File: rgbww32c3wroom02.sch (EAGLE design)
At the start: 21 parts, among them IC2 7805TV

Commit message: some corrections before production
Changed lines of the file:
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@@
 <instance part="R10" gate="G$1" x="-2.54" y="7.62" rot="R90"/>
 <instance part="GND1" gate="1" x="-55.88" y="114.3"/>
-<instance part="GND3" gate="1" x="-45.72" y="78.74"/>
+<instance part="GND3" gate="1" x="-55.88" y="73.66"/>
 <instance part="RST" gate="G$1" x="-88.9" y="78.74" smashed="yes">
 <attribute name="NAME" x="-83.82" y="76.2" size="1.778" layer="95" rot="R180"/>
@@
 <attribute name="VALUE" x="-101.6" y="35.56" size="1.778" layer="96"/>
 </instance>
-<instance part="U$5" gate="G$1" x="-63.5" y="63.5"/>
+<instance part="U$5" gate="G$1" x="-58.42" y="53.34"/>
 </instances>
 <busses>
@@
 </segment>
 <segment>
-<wire x1="-53.34" y1="81.28" x2="-45.72" y2="81.28" width="0.1524" layer="91"/>
+<wire x1="-60.96" y1="73.66" x2="-55.88" y2="76.2" width="0.1524" layer="91"/>
 <pinref part="GND3" gate="1" pin="GND"/>
 <pinref part="U$5" gate="G$1" pin="GND"/>
@@
 <net name="CLR" class="0">
 <segment>
-<wire x1="-40.64" y1="48.26" x2="-25.4" y2="48.26" width="0.1524" layer="91"/>
-<label x="-25.4" y="48.26" size="1.4224" layer="95" xref="yes"/>
+<wire x1="-48.26" y1="53.34" x2="-33.02" y2="53.34" width="0.1524" layer="91"/>
+<label x="-33.02" y="53.34" size="1.4224" layer="95" xref="yes"/>
 <pinref part="U$5" gate="G$1" pin="IO18"/>
 </segment>
@@
 <net name="N$5" class="0">
 <segment>
-<wire x1="-40.64" y1="63.5" x2="-25.4" y2="63.5" width="0.1524" layer="91"/>
-<label x="-25.4" y="63.5" size="1.4224" layer="95" xref="yes"/>
+<wire x1="-48.26" y1="60.96" x2="-38.1" y2="60.96" width="0.1524" layer="91"/>
+<label x="-38.1" y="60.96" size="1.4224" layer="95" xref="yes"/>
 <pinref part="U$5" gate="G$1" pin="I02"/>
 </segment>
@@
 <net name="N$9" class="0">
 <segment>
-<wire x1="-40.64" y1="53.34" x2="-25.4" y2="53.34" width="0.1524" layer="91"/>
-<label x="-25.4" y="53.34" size="1.4224" layer="95" xref="yes"/>
+<wire x1="-48.26" y1="55.88" x2="-38.1" y2="55.88" width="0.1524" layer="91"/>
+<label x="-38.1" y="55.88" size="1.4224" layer="95" xref="yes"/>
 <pinref part="U$5" gate="G$1" pin="IO19"/>
 </segment>
@@
 </segment>
 <segment>
-<wire x1="-60.96" y1="81.28" x2="-60.96" y2="88.9" width="0.1524" layer="91"/>
-<label x="-60.96" y="88.9" size="1.4224" layer="95" rot="R90" xref="yes"/>
+<wire x1="-63.5" y1="73.66" x2="-63.5" y2="78.74" width="0.1524" layer="91"/>
+<label x="-63.5" y="78.74" size="1.4224" layer="95" rot="R90" xref="yes"/>
 <pinref part="U$5" gate="G$1" pin="VCC"/>
 </segment>
@@
 <wire x1="-83.82" y1="78.74" x2="-83.82" y2="68.58" width="0.1524" layer="91"/>
 <pinref part="R6" gate="G$1" pin="2"/>
-<wire x1="-83.82" y1="68.58" x2="-73.66" y2="68.58" width="0.1524" layer="91"/>
+<wire x1="-83.82" y1="68.58" x2="-76.2" y2="63.5" width="0.1524" layer="91"/>
 <junction x="-83.82" y="68.58"/>
 <pinref part="U$5" gate="G$1" pin="EN"/>
@@
 <segment>
 <pinref part="U$5" gate="G$1" pin="IO8"/>
-<wire x1="-73.66" y1="43.18" x2="-88.9" y2="43.18" width="0.1524" layer="91"/>
+<wire x1="-76.2" y1="50.8" x2="-88.9" y2="43.18" width="0.1524" layer="91"/>
 <label x="-88.9" y="43.18" size="1.27" layer="95" rot="R180" xref="yes"/>
 </segment>
@@
 <segment>
 <pinref part="U$5" gate="G$1" pin="IO7"/>
-<wire x1="-73.66" y1="48.26" x2="-88.9" y2="48.26" width="0.1524" layer="91"/>
+<wire x1="-76.2" y1="53.34" x2="-88.9" y2="48.26" width="0.1524" layer="91"/>
 <label x="-88.9" y="48.26" size="1.27" layer="95" rot="R180" xref="yes"/>
 </segment>
@@
 <segment>
 <pinref part="U$5" gate="G$1" pin="IO6"/>
-<wire x1="-73.66" y1="53.34" x2="-88.9" y2="53.34" width="0.1524" layer="91"/>
+<wire x1="-76.2" y1="55.88" x2="-88.9" y2="53.34" width="0.1524" layer="91"/>
 <label x="-88.9" y="53.34" size="1.27" layer="95" rot="R180" xref="yes"/>
 </segment>
@@
 <segment>
 <pinref part="U$5" gate="G$1" pin="I05"/>
-<wire x1="-73.66" y1="58.42" x2="-88.9" y2="58.42" width="0.1524" layer="91"/>
+<wire x1="-76.2" y1="58.42" x2="-88.9" y2="58.42" width="0.1524" layer="91"/>
 <label x="-88.9" y="58.42" size="1.27" layer="95" rot="R180" xref="yes"/>
 </segment>
@@
 <segment>
 <pinref part="U$5" gate="G$1" pin="IO4"/>
-<wire x1="-73.66" y1="63.5" x2="-88.9" y2="63.5" width="0.1524" layer="91"/>
+<wire x1="-76.2" y1="60.96" x2="-88.9" y2="63.5" width="0.1524" layer="91"/>
 <label x="-88.9" y="63.5" size="1.27" layer="95" rot="R180" xref="yes"/>
 </segment>
@@
 </segment>
 <segment>
-<wire x1="-40.64" y1="43.18" x2="-25.4" y2="43.18" width="0.1524" layer="91"/>
-<label x="-25.4" y="43.18" size="1.778" layer="95" xref="yes"/>
+<wire x1="-48.26" y1="50.8" x2="-38.1" y2="50.8" width="0.1524" layer="91"/>
+<label x="-38.1" y="50.8" size="1.778" layer="95" xref="yes"/>
 <pinref part="U$5" gate="G$1" pin="TXD"/>
 </segment>
@@
 </segment>
 <segment>
-<wire x1="-40.64" y1="38.1" x2="-25.4" y2="38.1" width="0.1524" layer="91"/>
-<label x="-25.4" y="38.1" size="1.778" layer="95" xref="yes"/>
+<wire x1="-48.26" y1="48.26" x2="-33.02" y2="48.26" width="0.1524" layer="91"/>
+<label x="-33.02" y="48.26" size="1.778" layer="95" xref="yes"/>
 <pinref part="U$5" gate="G$1" pin="RXD"/>
 </segment>
@@
 </segment>
 <segment>
-<wire x1="-40.64" y1="73.66" x2="-25.4" y2="73.66" width="0.1524" layer="91"/>
-<label x="-25.4" y="73.66" size="1.4224" layer="95" xref="yes"/>
+<wire x1="-48.26" y1="66.04" x2="-33.02" y2="66.04" width="0.1524" layer="91"/>
+<label x="-33.02" y="66.04" size="1.4224" layer="95" xref="yes"/>
 <pinref part="U$5" gate="G$1" pin="IO0"/>
 </segment>
@@
 <segment>
 <pinref part="R7" gate="G$1" pin="2"/>
-<wire x1="-81.28" y1="38.1" x2="-73.66" y2="38.1" width="0.1524" layer="91"/>
+<wire x1="-81.28" y1="38.1" x2="-76.2" y2="48.26" width="0.1524" layer="91"/>
 <pinref part="U$5" gate="G$1" pin="IO9"/>
 </segment>

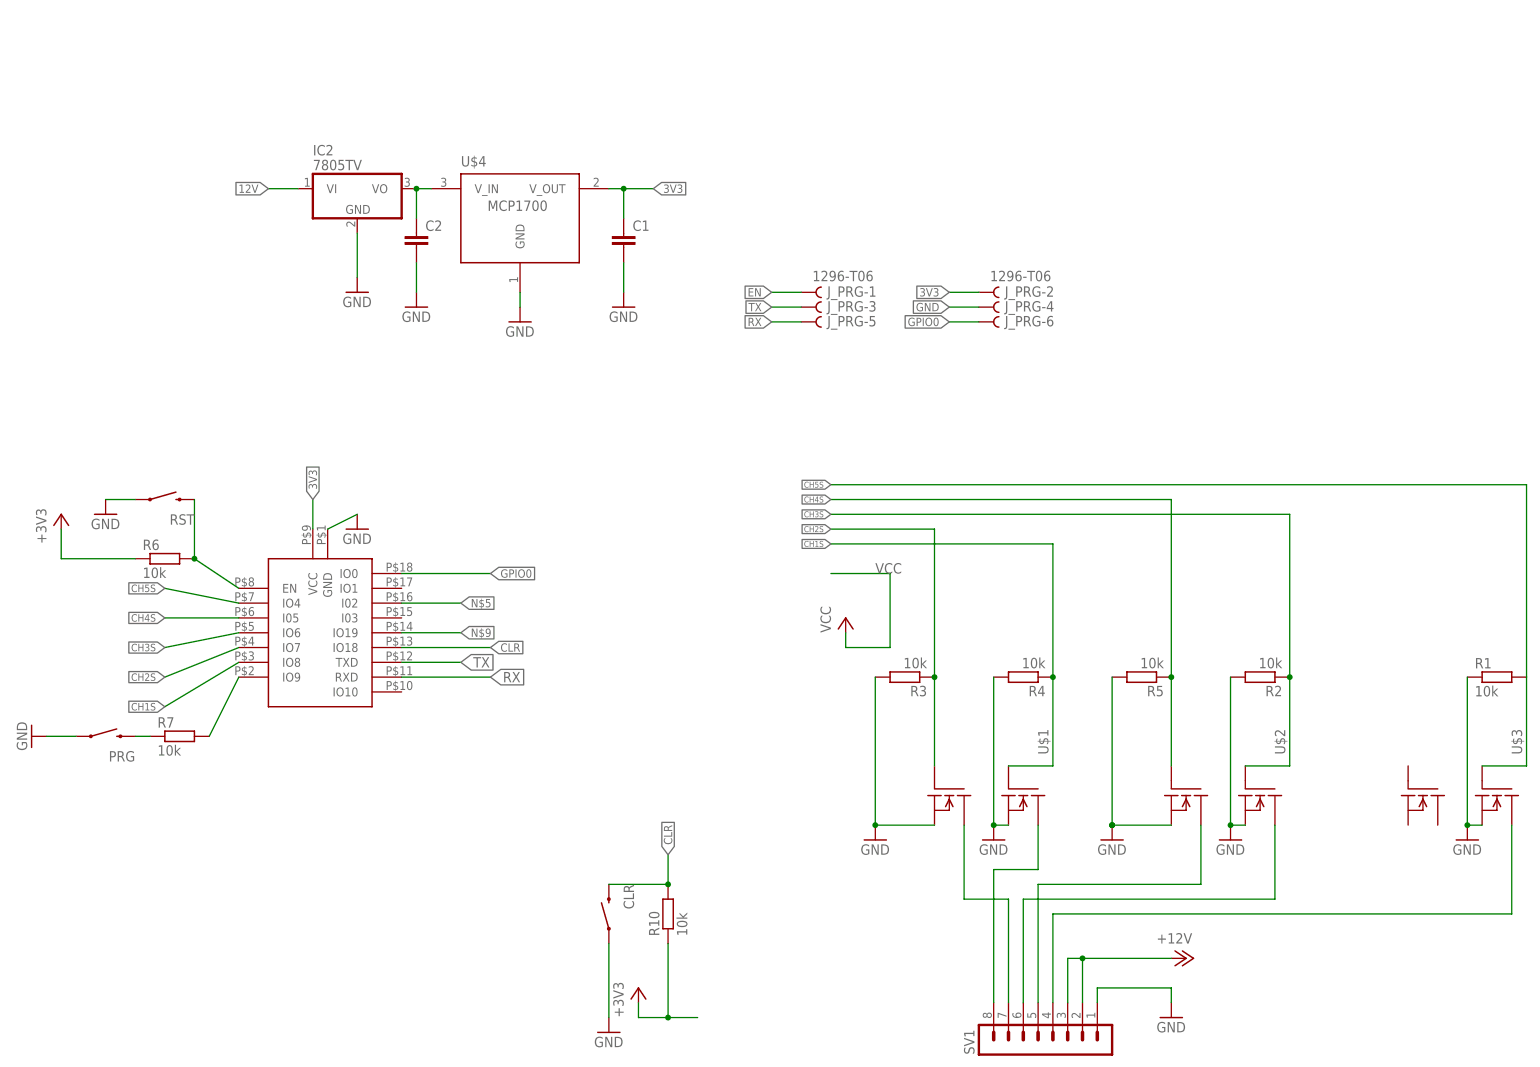
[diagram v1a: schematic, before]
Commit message: added local switching voltage regulator
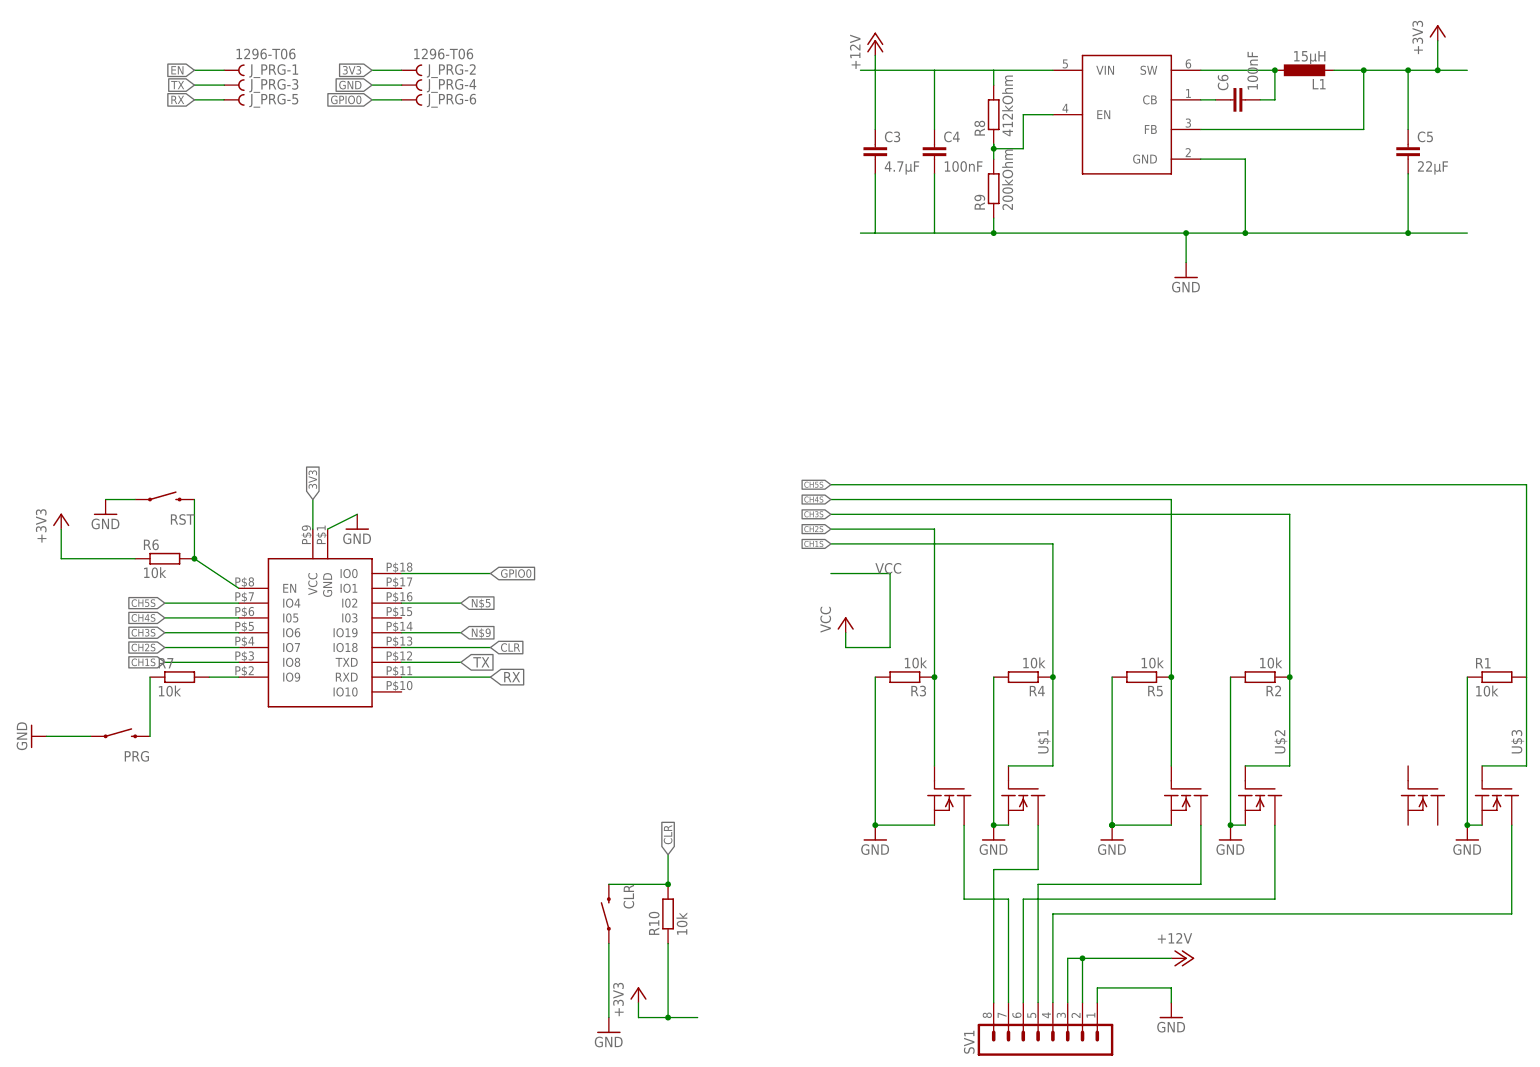
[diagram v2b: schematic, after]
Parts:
- removed C1, C2: (no value), rcl:C-EUC1206
- removed IC2: 7805TV, linear:7805TV
- removed U$4: MCP1700, MCP1700:MCP1700SOT23
- added C3: 4.7µF, rcl:C-EUC1210
- added C4, C6: 100nF, rcl:C-EUC0805
- added C5: 22µF, rcl:C-EUC0805
- added L1: 15µH, TI_Components:LPS4018
- added R8: 412kOhm, rcl:R-EU_M0805
- added R9: 200kOhm, rcl:R-EU_M0805
- added U$6: TPS5604030, TI_Components:TPS5604030
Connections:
- removed net 5V: C2.1, IC2.VO, U$4.V_IN
- new net BOOT: C6.1, U$6.CB
- new net EN_P: R8.1, R9.2, U$6.EN
- new net SW: C6.2, L1.1, U$6.SW
- net 12V: now also C3.1, C4.1, R8.2, U$6.VIN; no longer IC2.VI
- net 3V3: now also C5.1, L1.2, U$6.FB; no longer C1.1, U$4.V_OUT
- net GND: now also C3.2, C4.2, C5.2, R9.1, U$6.GND; no longer C1.2, C2.2, IC2.GND, U$4.GND
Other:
- moved on the sheet: J_PRG-1, J_PRG-2, J_PRG-3, J_PRG-4, J_PRG-5, J_PRG-6, PRG, R7
